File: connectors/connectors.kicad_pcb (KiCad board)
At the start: 2 copper layers, 41.7 x 4.8 mm, 20 parts, among them P11 CONN_1, P12 CONN_1, P13 CONN_1, P14 CONN_1, P15 CONN_1, P21 CONN_1, P22 CONN_1, P23 CONN_1, P24 CONN_1, P25 CONN_1

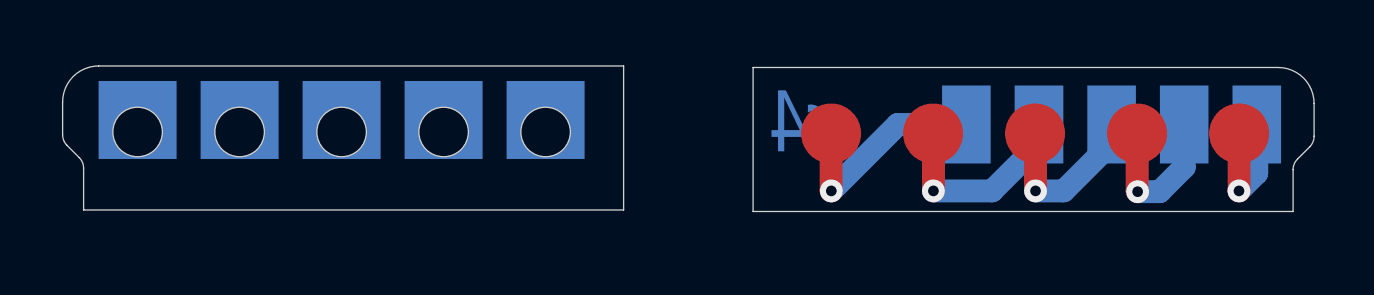
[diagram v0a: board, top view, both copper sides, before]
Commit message: Use 2 vias per pad. Fixes #36.
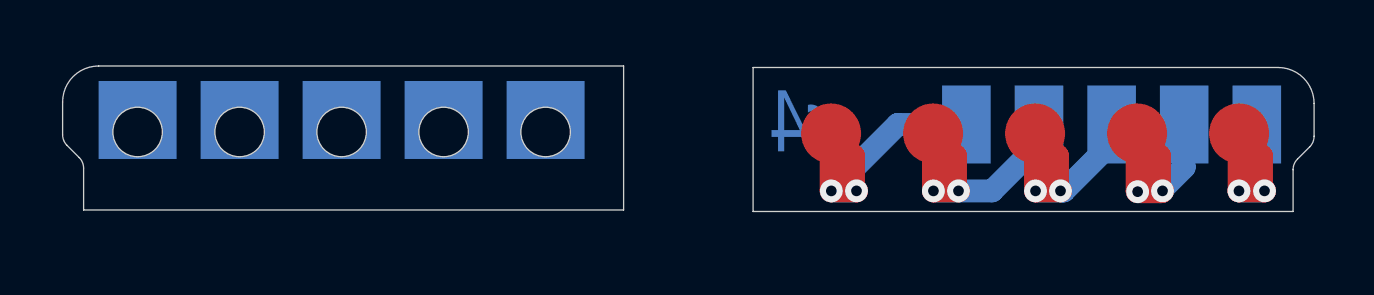
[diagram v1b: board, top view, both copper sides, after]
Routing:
- net N-000005: track 4.38 -> 8.34 mm, vias 1 -> 2
- net N-000001: track 7.34 -> 11.3 mm, vias 1 -> 2
- net N-000004: track 5.26 -> 8.47 mm, vias 1 -> 2
- net N-000003: track 5.76 -> 8.97 mm, vias 1 -> 2
- net N-000002: track 6.75 -> 9.86 mm, vias 1 -> 2
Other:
- net class Default: via_drill 0.381 -> 0.3556
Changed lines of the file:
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@@
     (thickness 1.6)
     (drawings 29)
-    (tracks 31)
+    (tracks 72)
     (zones 0)
     (modules 20)
@@
     (edge_width 0.01016)
     (via_size 0.762)
-    (via_drill 0.381)
+    (via_drill 0.3556)
     (via_min_size 0.762)
     (via_min_drill 0.3556)
@@
     (trace_width 0.762)
     (via_dia 0.762)
-    (via_drill 0.381)
+    (via_drill 0.3556)
     (uvia_dia 0.508)
     (uvia_drill 0.127)
+    (diff_pair_gap 0.25)
+    (diff_pair_width 0.762)
     (add_net N-000001)
     (add_net N-000002)
@@
   (gr_arc (start 156.853 108.287) (end 156.853 107.087) (angle 89.99995347) (layer Edge.Cuts) (width 0.01))
   (gr_line (start 158.053 109.379893) (end 158.053 108.287) (angle 90) (layer Edge.Cuts) (width 0.01))
+  (segment (start 141.9606 111.2012) (end 141.9618 111.2) (width 0.762) (layer B.Cu) (net 1))
+  (segment (start 141.9618 111.2) (end 142.8 111.2) (width 0.762) (layer B.Cu) (net 1))
+  (via (at 142.8 111.2) (size 0.762) (drill 0.3556) (layers F.Cu B.Cu) (net 1))
+  (segment (start 142.8 111.2) (end 142.7 111.1) (width 0.762) (layer F.Cu) (net 1))
+  (segment (start 142.7 111.1) (end 142.7 110.034) (width 0.762) (layer F.Cu) (net 1))
+  (segment (start 142.7 110.034) (end 141.953 109.287) (width 0.762) (layer F.Cu) (net 1))
   (segment (start 141.953 109.287) (end 141.953 111.1936) (width 0.762) (layer F.Cu) (net 1))
+  (segment (start 141.953 111.1936) (end 141.9606 111.2012) (width 0.762) (layer F.Cu) (net 1))
+  (segment (start 141.9618 111.2) (end 142.8 111.2) (width 0.762) (layer F.Cu) (net 1))
   (segment (start 144.1748 108.987) (end 146.463 108.987) (width 0.762) (layer B.Cu) (net 1))
   (segment (start 141.9606 111.2012) (end 144.1748 108.987) (width 0.762) (layer B.Cu) (net 1))
   (via (at 141.9606 111.2012) (size 0.762) (drill 0.3556) (layers F.Cu B.Cu) (net 1))
-  (segment (start 141.953 111.1936) (end 141.9606 111.2012) (width 0.762) (layer F.Cu) (net 1))
+  (segment (start 146.2 111.2) (end 146.1 111.1) (width 0.762) (layer F.Cu) (net 2))
+  (segment (start 146.1 110.034) (end 145.353 109.287) (width 0.762) (layer F.Cu) (net 2))
+  (segment (start 146.1 111.1) (end 146.1 110.034) (width 0.762) (layer F.Cu) (net 2))
+  (segment (start 145.3642 111.2012) (end 145.3654 111.2) (width 0.762) (layer F.Cu) (net 2))
+  (via (at 146.2 111.2) (size 0.762) (drill 0.3556) (layers F.Cu B.Cu) (net 2))
+  (segment (start 145.3654 111.2) (end 146.2 111.2) (width 0.762) (layer F.Cu) (net 2))
+  (segment (start 146.2 111.2) (end 146.2 111.2012) (width 0.762) (layer B.Cu) (net 2))
+  (segment (start 146.2 111.2012) (end 146.2 111.2) (width 0.762) (layer B.Cu) (net 2))
+  (segment (start 146.2 111.2) (end 146.2 111.2012) (width 0.762) (layer B.Cu) (net 2))
   (segment (start 145.353 109.287) (end 145.3642 109.2982) (width 0.762) (layer F.Cu) (net 2))
   (segment (start 145.3642 109.2982) (end 145.3642 111.2012) (width 0.762) (layer F.Cu) (net 2))
   (via (at 145.3642 111.2012) (size 0.762) (drill 0.3556) (layers F.Cu B.Cu) (net 2))
-  (segment (start 145.3642 111.2012) (end 147.32 111.2012) (width 0.762) (layer B.Cu) (net 2))
+  (segment (start 145.3642 111.2012) (end 146.2 111.2012) (width 0.762) (layer B.Cu) (net 2))
+  (segment (start 146.2 111.2012) (end 147.32 111.2012) (width 0.762) (layer B.Cu) (net 2))
   (segment (start 147.32 111.2012) (end 148.883 109.6382) (width 0.762) (layer B.Cu) (net 2))
   (segment (start 148.883 109.6382) (end 148.883 108.987) (width 0.762) (layer B.Cu) (net 2))
   (segment (start 148.8948 108.9988) (end 148.883 108.987) (width 0.762) (layer B.Cu) (net 2))
+  (segment (start 149.6 111.2) (end 149.5 111.1) (width 0.762) (layer F.Cu) (net 3))
+  (segment (start 149.5 111.1) (end 149.5 110.034) (width 0.762) (layer F.Cu) (net 3))
+  (segment (start 149.5 110.034) (end 148.753 109.287) (width 0.762) (layer F.Cu) (net 3))
+  (segment (start 148.7678 111.2012) (end 148.769 111.2) (width 0.762) (layer F.Cu) (net 3))
+  (segment (start 148.769 111.2) (end 149.6 111.2) (width 0.762) (layer F.Cu) (net 3))
+  (via (at 149.6 111.2) (size 0.762) (drill 0.3556) (layers F.Cu B.Cu) (net 3))
+  (segment (start 149.6 111.2) (end 149.6 111.2012) (width 0.762) (layer B.Cu) (net 3))
+  (segment (start 149.6 111.2012) (end 149.7076 111.2012) (width 0.762) (layer B.Cu) (net 3))
+  (via (at 148.7678 111.2012) (size 0.762) (drill 0.3556) (layers F.Cu B.Cu) (net 3))
+  (segment (start 148.7678 111.2012) (end 149.7076 111.2012) (width 0.762) (layer B.Cu) (net 3))
   (segment (start 148.753 109.287) (end 148.7678 109.3018) (width 0.762) (layer F.Cu) (net 3))
   (segment (start 148.7678 109.3018) (end 148.7678 111.2012) (width 0.762) (layer F.Cu) (net 3))
-  (via (at 148.7678 111.2012) (size 0.762) (drill 0.3556) (layers F.Cu B.Cu) (net 3))
-  (segment (start 148.7678 111.2012) (end 149.7076 111.2012) (width 0.762) (layer B.Cu) (net 3))
   (segment (start 149.7076 111.2012) (end 151.303 109.6058) (width 0.762) (layer B.Cu) (net 3))
   (segment (start 151.303 109.6058) (end 151.303 108.987) (width 0.762) (layer B.Cu) (net 3))
   (segment (start 151.2824 109.0076) (end 151.303 108.987) (width 0.762) (layer B.Cu) (net 3))
+  (segment (start 153 111.2) (end 152.9 111.1) (width 0.762) (layer F.Cu) (net 4))
+  (segment (start 152.9 110.034) (end 152.153 109.287) (width 0.762) (layer F.Cu) (net 4))
+  (segment (start 152.9 111.1) (end 152.9 110.034) (width 0.762) (layer F.Cu) (net 4))
+  (segment (start 152.1714 111.2266) (end 152.9734 111.2266) (width 0.762) (layer F.Cu) (net 4))
+  (segment (start 152.9734 111.2266) (end 153 111.2) (width 0.762) (layer F.Cu) (net 4))
+  (via (at 153 111.2) (size 0.762) (drill 0.3556) (layers F.Cu B.Cu) (net 4))
+  (segment (start 153 111.2) (end 152.9734 111.2266) (width 0.762) (layer B.Cu) (net 4))
+  (segment (start 152.9734 111.2266) (end 152.908 111.2266) (width 0.762) (layer B.Cu) (net 4))
+  (segment (start 152.1714 111.2266) (end 152.908 111.2266) (width 0.762) (layer B.Cu) (net 4))
+  (via (at 152.1714 111.2266) (size 0.762) (drill 0.3556) (layers F.Cu B.Cu) (net 4))
   (segment (start 152.153 109.287) (end 152.153 111.2082) (width 0.762) (layer F.Cu) (net 4))
+  (segment (start 152.153 111.2082) (end 152.1714 111.2266) (width 0.762) (layer F.Cu) (net 4))
   (segment (start 153.723 110.4116) (end 153.723 108.987) (width 0.762) (layer B.Cu) (net 4))
   (segment (start 152.908 111.2266) (end 153.723 110.4116) (width 0.762) (layer B.Cu) (net 4))
-  (segment (start 152.1714 111.2266) (end 152.908 111.2266) (width 0.762) (layer B.Cu) (net 4))
-  (via (at 152.1714 111.2266) (size 0.762) (drill 0.3556) (layers F.Cu B.Cu) (net 4))
-  (segment (start 152.153 111.2082) (end 152.1714 111.2266) (width 0.762) (layer F.Cu) (net 4))
   (segment (start 153.7208 108.9892) (end 153.723 108.987) (width 0.762) (layer B.Cu) (net 4))
+  (segment (start 156.4 111.2) (end 156.3 111.1) (width 0.762) (layer F.Cu) (net 5))
+  (segment (start 156.3 110.034) (end 155.553 109.287) (width 0.762) (layer F.Cu) (net 5))
+  (segment (start 156.3 111.1) (end 156.3 110.034) (width 0.762) (layer F.Cu) (net 5))
+  (segment (start 156.4 111.2) (end 155.5508 111.2) (width 0.762) (layer B.Cu) (net 5))
+  (segment (start 156.3988 111.2012) (end 156.4 111.2) (width 0.762) (layer F.Cu) (net 5))
+  (via (at 156.4 111.2) (size 0.762) (drill 0.3556) (layers F.Cu B.Cu) (net 5))
+  (segment (start 155.5496 111.2012) (end 156.3988 111.2012) (width 0.762) (layer F.Cu) (net 5))
+  (segment (start 155.5508 111.2) (end 155.5496 111.2012) (width 0.762) (layer B.Cu) (net 5))
   (segment (start 155.553 109.287) (end 155.553 111.1978) (width 0.762) (layer F.Cu) (net 5))
   (segment (start 155.553 111.1978) (end 155.5496 111.2012) (width 0.762) (layer F.Cu) (net 5))

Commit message: Redesign the pitch and space of the female vertical PCB inner pads according to the newly available space.
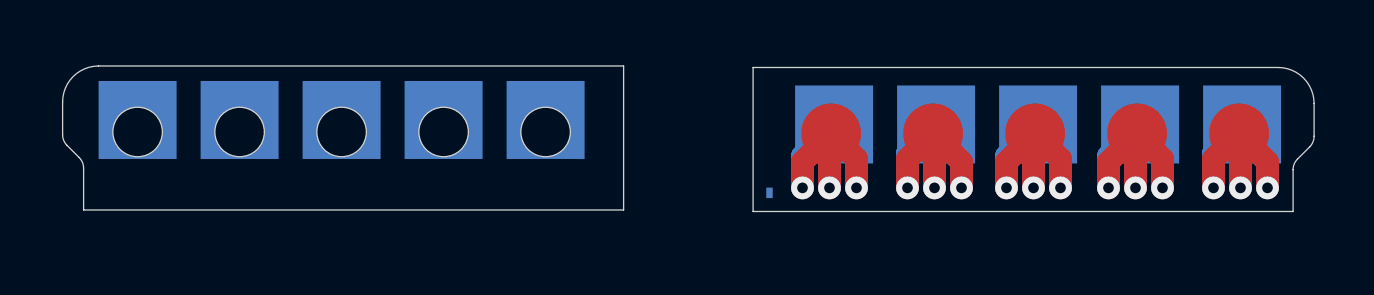
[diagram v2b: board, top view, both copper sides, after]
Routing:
- net N-000005: track 8.34 -> 13.3 mm, vias 2 -> 3
- net N-000004: track 8.47 -> 13.4 mm, vias 2 -> 3
- net N-000003: track 8.97 -> 13.4 mm, vias 2 -> 3
- net N-000002: track 9.86 -> 13.3 mm, vias 2 -> 3
- net N-000001: track 11.3 -> 13.4 mm, vias 2 -> 3
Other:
- board text added: "."
- board text removed: "r4"

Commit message: Update connector footprints.
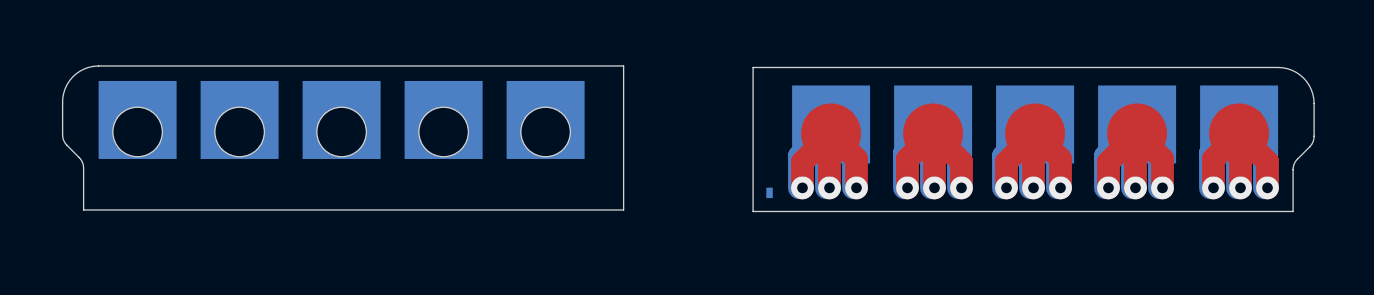
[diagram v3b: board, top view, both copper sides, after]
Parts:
- moved P22 0.10 mm to (148.8, 109.0)
- moved P24 0.10 mm to (153.6, 109.0)
- moved P21 0.10 mm to (146.4, 109.0)
- moved P23 0.10 mm to (151.2, 109.0)
- moved P25 0.10 mm to (156.0, 109.0)

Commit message: Align connectors to the 0.1mm grid.
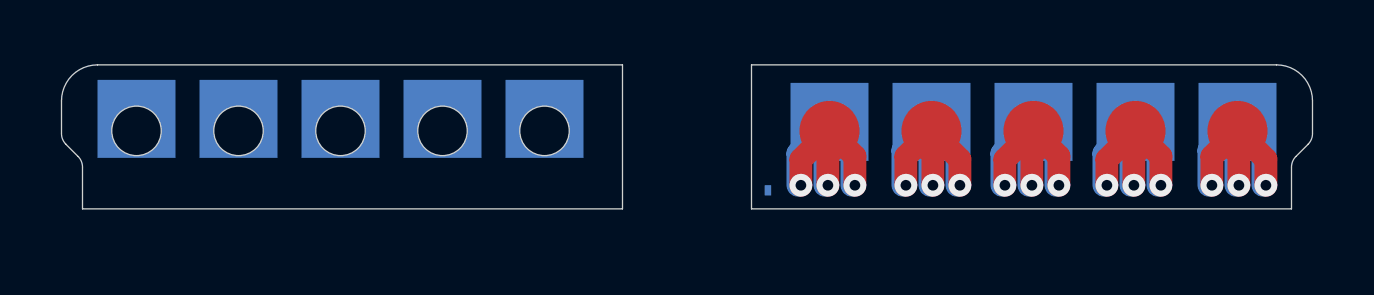
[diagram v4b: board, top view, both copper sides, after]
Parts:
- moved P11 0.10 mm to (141.9, 109.2)
- moved P12 0.10 mm to (145.3, 109.2)
- moved P13 0.10 mm to (148.7, 109.2)
- moved P14 0.10 mm to (152.1, 109.2)
- moved P15 0.10 mm to (155.5, 109.2)
- moved P21 0.10 mm to (146.3, 108.9)
- moved P22 0.10 mm to (148.7, 108.9)
- moved P23 0.10 mm to (151.2, 108.9)
- moved P24 0.10 mm to (153.6, 108.9)
- moved P25 0.10 mm to (156.0, 108.9)
- moved REF** 0.05 mm to (132.4, 108.8)
- moved REF** 0.05 mm to (125.6, 108.8)
- moved REF** 0.05 mm to (129.0, 108.8)
- moved REF** 0.05 mm to (122.2, 108.8)
- moved REF** 0.05 mm to (118.8, 109.2)
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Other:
- outline, holes or cut-outs redrawn

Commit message: Add zones near the pads and around the vias.
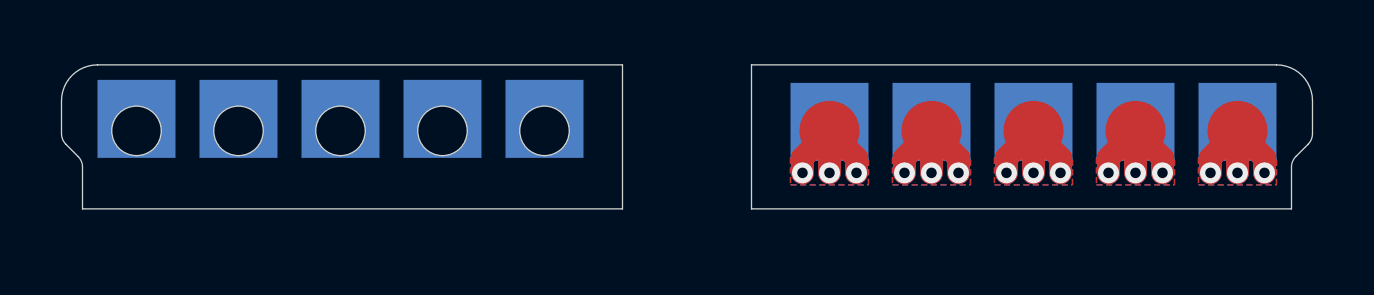
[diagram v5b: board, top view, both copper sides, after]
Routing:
- net N-000005: track 13.3 -> 10.9 mm
- net N-000003: track 13.4 -> 11.1 mm
- net N-000004: track 13.4 -> 11.1 mm
- net N-000001: track 13.4 -> 11.9 mm
- net N-000002: track 13.3 -> 12.1 mm
- added copper zone on B.Cu, net N-000001
- added copper zone on F.Cu, net N-000001
- added copper zone on B.Cu, net N-000002
- added copper zone on F.Cu, net N-000002
- added copper zone on B.Cu, net N-000003
- added copper zone on F.Cu, net N-000003
- added copper zone on B.Cu, net N-000004
- added copper zone on F.Cu, net N-000004
- added copper zone on B.Cu, net N-000005
- added copper zone on F.Cu, net N-000005
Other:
- net class Default: via_dia 0.762 -> 0.7; via_drill 0.3556 -> 0.35
- rule via_min_drill: 0.3556 -> 0.35
- rule via_min_size: 0.762 -> 0.7
- board text removed: "."

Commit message: Update connector contours.
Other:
- outline, holes or cut-outs redrawn
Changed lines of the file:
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@@
       (net 5 N-000005))
   )
+  (gr_line (start 117 110.614214) (end 117 111.8) (layer Edge.Cuts) (width 0.1))
+  (gr_line (start 117 111.8) (end 135 111.8) (layer Edge.Cuts) (width 0.1))
+  (gr_line (start 135 111.8) (end 135 107) (layer Edge.Cuts) (width 0.1))
+  (gr_line (start 135 107) (end 117.5 107) (layer Edge.Cuts) (width 0.1))
+  (gr_arc (start 117.5 108.2) (end 117.5 107) (angle -90) (layer Edge.Cuts) (width 0.1))
+  (gr_line (start 116.3 108.2) (end 116.3 109.292893) (layer Edge.Cuts) (width 0.1))
+  (gr_arc (start 116 110.614214) (end 117 110.614214) (angle -45) (layer Edge.Cuts) (width 0.1))
+  (gr_line (start 116.446447 109.646447) (end 116.707107 109.907107) (layer Edge.Cuts) (width 0.1))
+  (gr_arc (start 116.8 109.292893) (end 116.3 109.292893) (angle -45) (layer Edge.Cuts) (width 0.1))
+  (gr_line (start 157.3 110.614214) (end 157.3 111.8) (layer Edge.Cuts) (width 0.1))
+  (gr_line (start 157.3 111.8) (end 139.3 111.8) (layer Edge.Cuts) (width 0.1))
+  (gr_line (start 139.3 111.8) (end 139.3 107) (layer Edge.Cuts) (width 0.1))
+  (gr_line (start 139.3 107) (end 156.8 107) (layer Edge.Cuts) (width 0.1))
+  (gr_arc (start 156.8 108.2) (end 158 108.2) (angle -90) (layer Edge.Cuts) (width 0.1))
+  (gr_line (start 158 108.2) (end 158 109.292893) (layer Edge.Cuts) (width 0.1))
+  (gr_arc (start 157.5 109.292893) (end 157.853553 109.646447) (angle -45) (layer Edge.Cuts) (width 0.1))
+  (gr_line (start 157.853553 109.646447) (end 157.592893 109.907107) (layer Edge.Cuts) (width 0.1))
+  (gr_arc (start 158.3 110.614214) (end 157.592893 109.907107) (angle -45) (layer Edge.Cuts) (width 0.1))
   (dimension 4.8006 (width 0.3) (layer Cmts.User)
     (gr_text " " (at 112.6755 109.3989 90) (layer Cmts.User)
@@
     (arrow2b (pts (xy 116.30008 102.00242) (xy 117.426584 101.415999)))
   )
-  (gr_line (start 116.3 109.292893) (end 116.3 108.2) (angle 90) (layer Edge.Cuts) (width 0.01))
-  (gr_arc (start 117.5 108.2) (end 117.5 107) (angle -89.99995347) (layer Edge.Cuts) (width 0.01))
-  (gr_line (start 117.5 107) (end 135 107) (angle 90) (layer Edge.Cuts) (width 0.01))
-  (gr_line (start 135 107) (end 135 111.8) (angle 90) (layer Edge.Cuts) (width 0.01))
-  (gr_line (start 135 111.8) (end 117 111.8) (angle 90) (layer Edge.Cuts) (width 0.01))
-  (gr_line (start 117 111.8) (end 117 110.407107) (angle 90) (layer Edge.Cuts) (width 0.01))
-  (gr_line (start 116.853553 110.053553) (end 116.446447 109.646447) (angle 90) (layer Edge.Cuts) (width 0.01))
-  (gr_arc (start 116.5 110.407107) (end 117 110.407107) (angle -45.00015451) (layer Edge.Cuts) (width 0.01))
-  (gr_arc (start 116.8 109.292893) (end 116.3 109.292893) (angle -44.99944414) (layer Edge.Cuts) (width 0.01))
   (gr_text "4.8 mm = 0.189 in" (at 102.09132 109.24396) (layer Cmts.User)
     (effects (font (size 1.5 1.5) (thickness 0.3)))
@@
     (effects (font (size 1.5 1.5) (thickness 0.3)))
   )
-  (gr_arc (start 157.5 109.292893) (end 158 109.292893) (angle 44.99944414) (layer Edge.Cuts) (width 0.01))
-  (gr_arc (start 157.8 110.407107) (end 157.3 110.407107) (angle 45.00015451) (layer Edge.Cuts) (width 0.01))
-  (gr_line (start 157.446447 110.053553) (end 157.853553 109.646447) (angle 90) (layer Edge.Cuts) (width 0.01))
-  (gr_line (start 157.3 111.8) (end 157.3 110.407107) (angle 90) (layer Edge.Cuts) (width 0.01))
-  (gr_line (start 139.3 111.8) (end 157.3 111.8) (angle 90) (layer Edge.Cuts) (width 0.01))
-  (gr_line (start 139.3 107) (end 139.3 111.8) (angle 90) (layer Edge.Cuts) (width 0.01))
-  (gr_line (start 156.8 107) (end 139.3 107) (angle 90) (layer Edge.Cuts) (width 0.01))
-  (gr_arc (start 156.8 108.2) (end 156.8 107) (angle 89.99995347) (layer Edge.Cuts) (width 0.01))
-  (gr_line (start 158 109.292893) (end 158 108.2) (angle 90) (layer Edge.Cuts) (width 0.01))
   (segment (start 141.9 108.9) (end 141 109.8) (width 0.762) (layer B.Cu) (net 1))
   (segment (start 141 109.8) (end 141 110.6) (width 0.762) (layer B.Cu) (net 1))

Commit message: Update surface finish to hard gold.
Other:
- board text added: "design is 30mil-10mil-14mil trace-clearance-minimum_drill 2.5mm board thickness black solder mask hard gold finish no silk screen"
- board text removed: "design is 30mil-10mil-14mil trace-clearance-minimum_drill 2.5mm board thickness black solder mask ENIG finish no silk screen"
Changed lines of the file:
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@@
     (effects (font (size 1.5 1.5) (thickness 0.3)))
   )
-  (gr_text "design is 30mil-10mil-14mil trace-clearance-minimum_drill\n2.5mm board thickness\nblack solder mask\nENIG finish\nno silk screen" (at 99.1754 87.7073) (layer Cmts.User)
+  (gr_text "design is 30mil-10mil-14mil trace-clearance-minimum_drill\n2.5mm board thickness\nblack solder mask\nhard gold finish\nno silk screen" (at 99.1754 87.7073) (layer Cmts.User)
     (effects (font (size 1.5 1.5) (thickness 0.3)) (justify left))
   )
